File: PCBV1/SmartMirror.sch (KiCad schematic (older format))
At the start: 0 parts

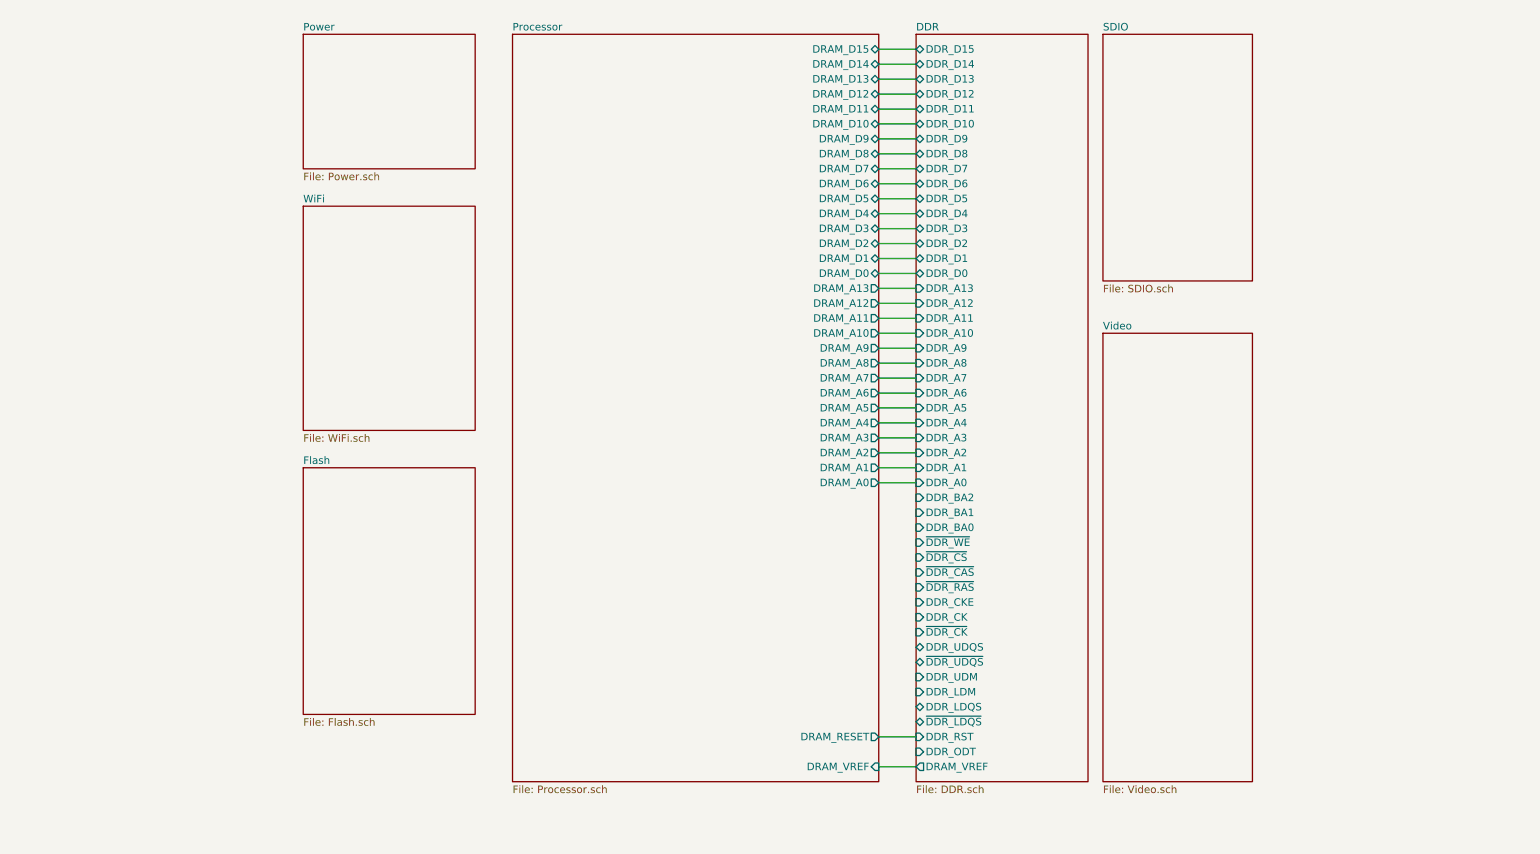
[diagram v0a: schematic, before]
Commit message: Added UART, modifications to video etc.
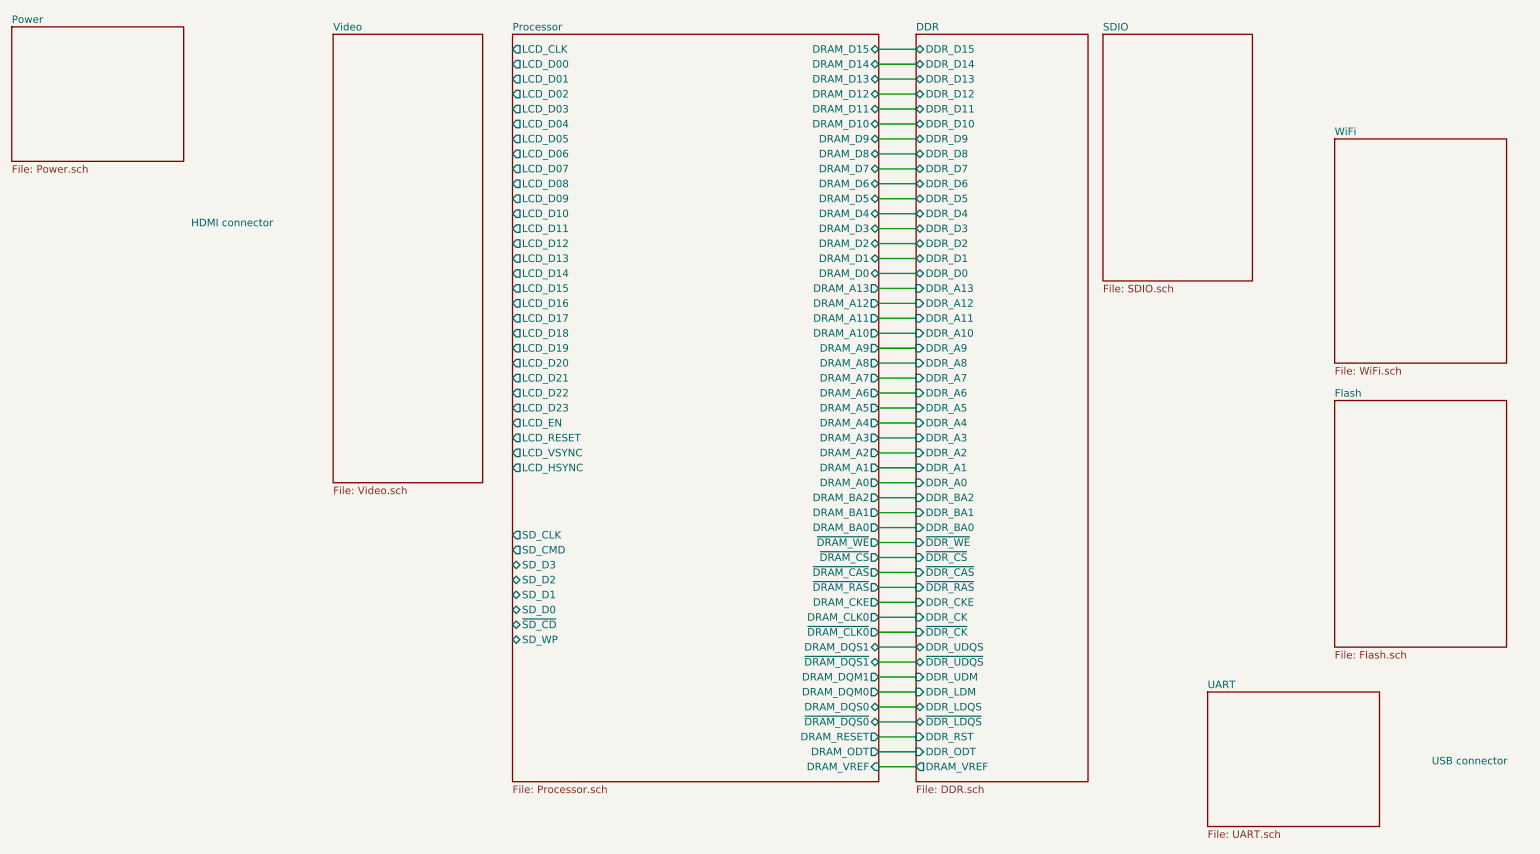
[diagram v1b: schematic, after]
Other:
- note added: "HDMI connector"
- note added: "USB connector"
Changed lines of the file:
@@
 $Descr A4 11693 8268
 encoding utf-8
-Sheet 1 8
+Sheet 1 9
 Title "Smart Mirror"
 Date "2021-01-21"
@@
 $EndDescr
 $Sheet
-S 2800 2000 1150 1500
+S 9700 1550 1150 1500
 U 6009E54D
 F0 "WiFi" 50
@@
 $EndSheet
 $Sheet
-S 8150 2850 1000 3000
+S 3000 850  1000 3000
 U 6009E791
 F0 "Video" 50
@@
 $EndSheet
 $Sheet
-S 2800 3750 1150 1650
+S 9700 3300 1150 1650
 U 6009E7FD
 F0 "Flash" 50
@@
 $EndSheet
 $Sheet
-S 2800 850  1150 900
+S 850  800  1150 900
 U 60251FB2
 F0 "Power" 50
@@
 F32 "DRAM_A7" O R 6650 3150 50
 F33 "DRAM_A8" O R 6650 3050 50
+F34 "~DRAM_CLK0" O R 6650 4850 50
+F35 "DRAM_CLK0" O R 6650 4750 50
+F36 "~DRAM_CS" O R 6650 4350 50
+F37 "DRAM_ODT" O R 6650 5650 50
+F38 "DRAM_CKE" O R 6650 4650 50
+F39 "DRAM_BA0" O R 6650 4150 50
+F40 "~DRAM_RAS" O R 6650 4550 50
+F41 "DRAM_BA2" O R 6650 3950 50
+F42 "~DRAM_CAS" O R 6650 4450 50
+F43 "~DRAM_WE" O R 6650 4250 50
+F44 "DRAM_BA1" O R 6650 4050 50
+F45 "~DRAM_DQS0" B R 6650 5450 50
+F46 "DRAM_DQS0" B R 6650 5350 50
+F47 "DRAM_DQM0" O R 6650 5250 50
+F48 "DRAM_DQM1" O R 6650 5150 50
+F49 "~DRAM_DQS1" B R 6650 5050 50
+F50 "DRAM_DQS1" B R 6650 4950 50
+F51 "SD_CLK" O L 4200 4200 50
+F52 "SD_CMD" O L 4200 4300 50
+F53 "SD_D2" B L 4200 4500 50
+F54 "SD_D1" B L 4200 4600 50
+F55 "SD_D0" B L 4200 4700 50
+F56 "SD_D3" B L 4200 4400 50
+F57 "~SD_CD" B L 4200 4800 50
+F58 "SD_WP" B L 4200 4900 50
+F59 "LCD_CLK" O L 4200 950 50
+F60 "LCD_D01" O L 4200 1150 50
+F61 "LCD_D06" O L 4200 1650 50
+F62 "LCD_D09" O L 4200 1950 50
+F63 "LCD_D14" O L 4200 2450 50
+F64 "LCD_D18" O L 4200 2850 50
+F65 "LCD_D22" O L 4200 3250 50
+F66 "LCD_EN" O L 4200 3450 50
+F67 "LCD_D00" O L 4200 1050 50
+F68 "LCD_D05" O L 4200 1550 50
+F69 "LCD_D08" O L 4200 1850 50
+F70 "LCD_D13" O L 4200 2350 50
+F71 "LCD_D17" O L 4200 2750 50
+F72 "LCD_D21" O L 4200 3150 50
+F73 "LCD_D23" O L 4200 3350 50
+F74 "LCD_D04" O L 4200 1450 50
+F75 "LCD_D12" O L 4200 2250 50
+F76 "LCD_D16" O L 4200 2650 50
+F77 "LCD_D20" O L 4200 3050 50
+F78 "LCD_VSYNC" O L 4200 3650 50
+F79 "LCD_HSYNC" O L 4200 3750 50
+F80 "LCD_D03" O L 4200 1350 50
+F81 "LCD_D07" O L 4200 1750 50
+F82 "LCD_D11" O L 4200 2150 50
+F83 "LCD_D15" O L 4200 2550 50
+F84 "LCD_D19" O L 4200 2950 50
+F85 "LCD_D02" O L 4200 1250 50
+F86 "LCD_D10" O L 4200 2050 50
+F87 "LCD_RESET" O L 4200 3550 50
 $EndSheet
 Wire Wire Line
@@
 Wire Wire Line
 	6650 2550 6900 2550
+$Sheet
+S 8850 5250 1150 900
+U 613369D9
+F0 "UART" 50
+F1 "UART.sch" 50
+$EndSheet
+Wire Wire Line
+	6650 5650 6900 5650
+Wire Wire Line
+	6900 4850 6650 4850
+Wire Wire Line
+	6650 4750 6900 4750
+Wire Wire Line
+	6900 4650 6650 4650
+Wire Wire Line
+	6650 4550 6900 4550
+Wire Wire Line
+	6900 4450 6650 4450
+Wire Wire Line
+	6650 4350 6900 4350
+Wire Wire Line
+	6900 4250 6650 4250
+Wire Wire Line
+	6650 4150 6900 4150
+Wire Wire Line
+	6900 4050 6650 4050
+Wire Wire Line
+	6650 3950 6900 3950
+Wire Wire Line
+	6650 4950 6900 4950
+Wire Wire Line
+	6900 5050 6650 5050
+Wire Wire Line
+	6650 5150 6900 5150
+Wire Wire Line
+	6900 5250 6650 5250
+Wire Wire Line
+	6650 5350 6900 5350
+Wire Wire Line
+	6900 5450 6650 5450
+Text Notes 2050 2150 0    50   ~ 0
+HDMI connector
+Text Notes 10350 5750 0    50   ~ 0
+USB connector
 $EndSCHEMATC
